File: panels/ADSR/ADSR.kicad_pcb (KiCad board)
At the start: 2 copper layers, 70.8 x 128.4 mm, 12 parts

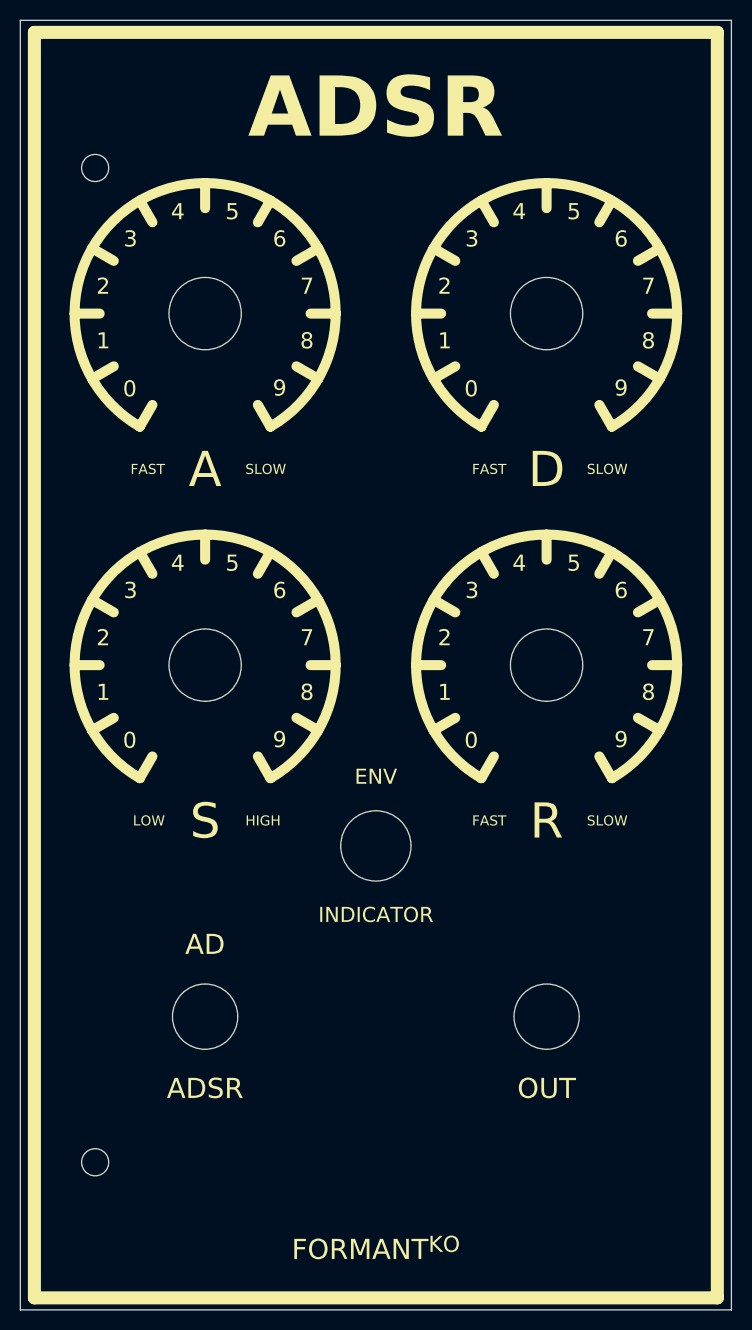
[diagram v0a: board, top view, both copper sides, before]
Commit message: updated adsr/dual vca
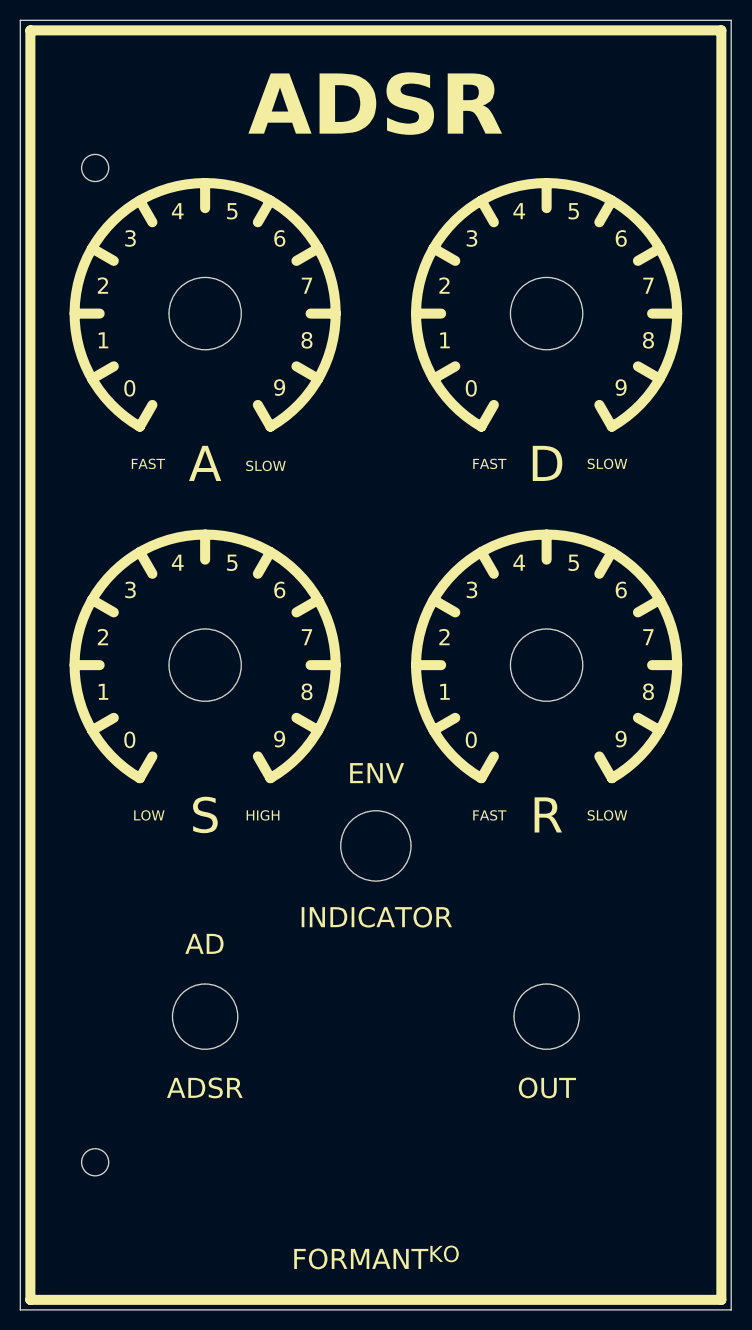
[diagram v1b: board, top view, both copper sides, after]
